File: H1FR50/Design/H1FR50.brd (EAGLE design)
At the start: 34.6 x 60 mm, 49 parts, among them J1 MOLEX_INC_0732511150MOLEX_INC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, P1 HEXABIT_17.32_X2_NO_P5, U1 STM32F091RBT6STMICROELECTRONI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, U2 TPS22943DCKR, U3 BGA824N6, U4 TESEO-LIV3F, U5 B39162B4327P810, X1 XTALL_CSTCE8M00G52

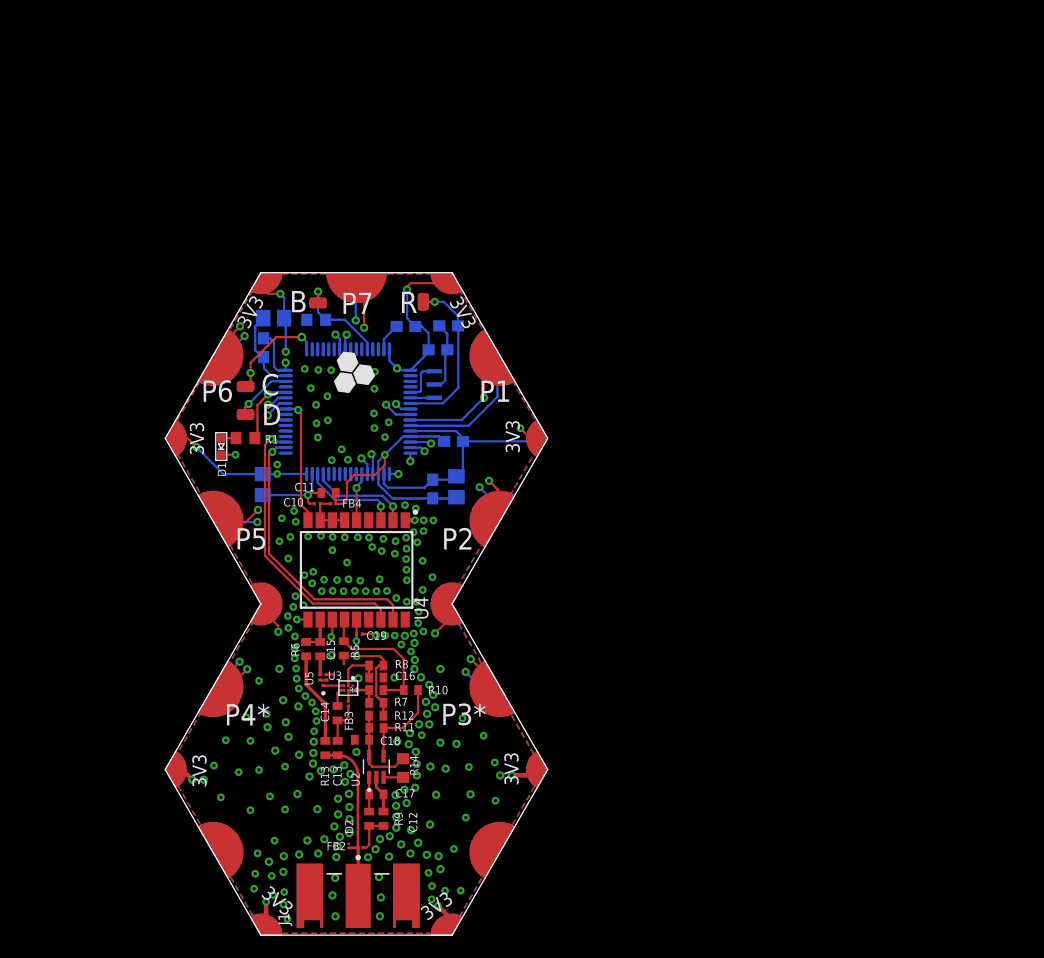
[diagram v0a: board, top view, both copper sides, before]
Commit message: -Changing the MC to STM32G0B1CEU6N -Changing the GPS Module to SAM-M8Q-0-10 u-blox
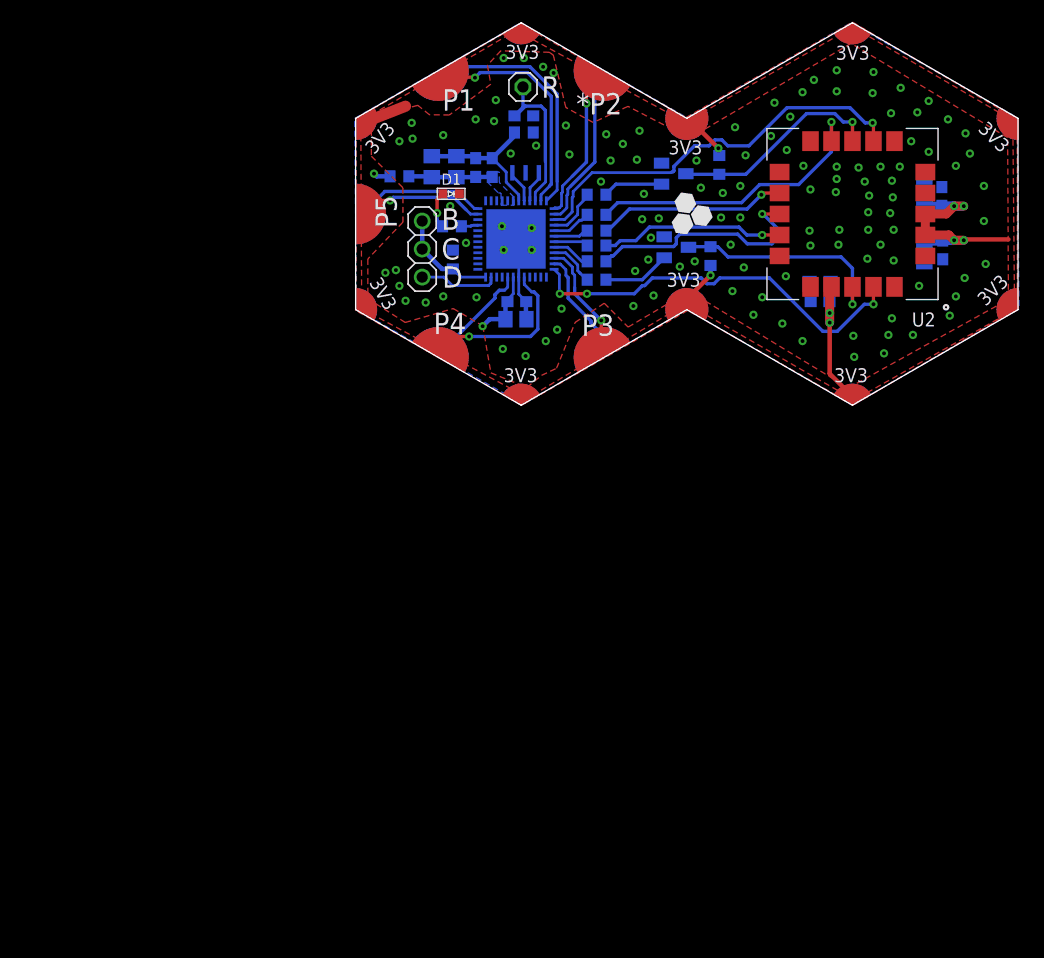
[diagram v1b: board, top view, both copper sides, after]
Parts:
- removed B, C, D, R: PAD1, Hexabitz:PAD1
- removed C14: 3.9pF, HEXABITZ_RCLS:C-0402
- removed C15: 120pF, HEXABITZ_RCLS:C-0402
- removed C16: 1nF, HEXABITZ_RCLS:C-0402
- removed C17: 1.00uF, HEXABITZ_RCLS:C-0402
- removed C18: 2.2uF, HEXABITZ_RCLS:C-0402
- removed C19: 56pF, HEXABITZ_RCLS:C-0201
- removed D2: ESDARF02-1BU2CK, HEXABITZ_RCLS:CAPC0201X13N
- removed FB4: 27nH, HEXABITZ_RCLS:FB-0402
- removed J1: MOLEX_INC_0732511150MOLEX_INC_0732511150_0_0, HEXABITZ_CONNECTION_PARTS:MOLEX_INC_0732511150_0
- removed P1: HEXABIT_17.32_X2_NO_P5, hexabitz_connectors:HEXABIT_17.32_X2_NO_P5
- removed R10, R12: 0.0R, HEXABITZ_RCLS:R-0402
- removed R11, R13: DNP, HEXABITZ_RCLS:R-0402
- removed R14: 100k, HEXABITZ_RCLS:R-0603
- removed U3: BGA824N6, HEXABITZ_ICs:BGA824N6
- removed U4: TESEO-LIV3F, HEXABITZ_ICs:SON110P970X1010X230-18N
- removed U5: B39162B4327P810, HEXABITZ_ICs:FIL_B39162B4327P810
- added FB1: (no value), HEXABITZ_RCLS:FB-0603
- added JP1: R, HEXABITZ_USER_INTERFACE_PARTS:1X01
- added JP2: (no value), pinhead:1X03
- added P2: HEXABIT_X2_P1_P5, hexabitz_connectors:HEXABIT_17.32_X2_P1_P5
- added Q1, Q2: MMBT3904LT1, HEXABITZ_RCLS:MMBT3904LT1
- added R3: 270R, HEXABITZ_RCLS:R-0603
- C1: value 10nF -> 100nF; device Hexabitz:C-0603 -> HEXABITZ_RCLS:C-0603
- C10: value 56pF -> 100nF; device HEXABITZ_RCLS:C-0201 -> HEXABITZ_RCLS:C-0603
- C11: value 10nF -> 4.7uF; device HEXABITZ_RCLS:C-0402 -> HEXABITZ_RCLS:C-0805-POL
- C12: value 56pF -> 100nF; device HEXABITZ_RCLS:C-0402 -> HEXABITZ_RCLS:C-0603
- C13: value 120pF -> 4.7uF; device HEXABITZ_RCLS:C-0402 -> HEXABITZ_RCLS:C-0805-POL
- C2: value 1.00uF -> 4.7uF; device Hexabitz:C-0805-POL -> HEXABITZ_RCLS:C-0805-POL
- C3, C5, C6, C8: device Hexabitz:C-0603 -> HEXABITZ_RCLS:C-0603
- C4: value 4.7uF -> 1uF; device Hexabitz:C-0805-POL -> HEXABITZ_RCLS:C-0805-POL
- C7: device Hexabitz:C-0805-POL -> HEXABITZ_RCLS:C-0805-POL
- C9: value 100nF -> 4.7uF; device Hexabitz:C-0603 -> HEXABITZ_RCLS:C-0805-POL
- FB2: value 56nH -> BLM18KG601SN1D; device HEXABITZ_RCLS:FB-0402 -> HEXABITZ_RCLS:FB-0603
- FB3: value 6.8nH -> BLM18KG601SN1D; device HEXABITZ_RCLS:FB-0402 -> HEXABITZ_RCLS:FB-0603
- R1: value 270.0R -> 10K; device Hexabitz:R-0603 -> HEXABITZ_RCLS:R-0603
- R2: value 10.0K -> 0.0R; device Hexabitz:R-0603 -> HEXABITZ_RCLS:R-0603
- R4: value 0.0R -> 10K; device HEXABITZ_RCLS:R-0402 -> HEXABITZ_RCLS:R-0603
- R5: value 10.0k -> 10K; device HEXABITZ_RCLS:R-0402 -> HEXABITZ_RCLS:R-0603
- R6, R7: value DNP -> 10K; device HEXABITZ_RCLS:R-0402 -> HEXABITZ_RCLS:R-0603
- R8: value 0.0R -> 150R; device HEXABITZ_RCLS:R-0402 -> HEXABITZ_RCLS:R-0603
- R9: value DNP -> 150R; device HEXABITZ_RCLS:R-0402 -> HEXABITZ_RCLS:R-0603
- U1: value STM32F091RBT6STMICROELECTRONICS_STM32F091RBT6_0_1 -> STM32G0B1CEU6NUFQFPN48_STM32_STM; device Hexabitz:STMICROELECTRONICS_STM32F091RBT6_1 -> HEXABITZ_ICs:UFQFPN48_STM32_STM
- U2: value TPS22943DCKR -> SAM-M8Q-0-10; device HEXABITZ_ICs:SOT65P210X110-5N -> SAM-M8Q-0-10:MODULE_SAM-M8Q-0-10
- moved U2 66.1 mm to (44.9, 20.3), turned to 180 degrees
- moved C10 63.0 mm to (53.0, 21.9), flipped to the bottom, turned to 90 degrees
- moved C12 61.3 mm to (42.0, 12.4), flipped to the bottom, turned to 0 degrees
- moved C13 60.6 mm to (42.0, 14.0), flipped to the bottom, turned to 0 degrees
- moved C11 60.3 mm to (51.4, 22.0), flipped to the bottom, turned to 90 degrees
- moved FB2 58.6 mm to (21.7, 17.5), flipped to the bottom, turned to 0 degrees
- moved R9 58.4 mm to (21.7, 20.2), flipped to the bottom, turned to 0 degrees
- moved R6 57.6 mm to (32.9, 24.8), flipped to the bottom
- moved R7 50.5 mm to (32.1, 16.5), flipped to the bottom, turned to 270 degrees
- moved R5 47.0 mm to (21.7, 22.1), flipped to the bottom, turned to 0 degrees
- moved FB3 45.9 mm to (21.7, 16.0), flipped to the bottom, turned to 0 degrees
- moved C8 45.3 mm to (53.1, 17.1), turned to 270 degrees
- moved C9 44.9 mm to (51.4, 16.9), turned to 270 degrees
- moved R8 44.2 mm to (21.7, 18.8), flipped to the bottom
- moved R4 42.2 mm to (21.7, 14.4), flipped to the bottom
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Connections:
- removed net ANTOFF: R10.2, R4.2, R5.1, U4.13
- removed net ANT_IN: R13.1, R6.1
- removed net B1: B.P$1, B.P$2, R2.2, U1.60
- removed net I2C_CLOCK: U1.34, U4.17
- removed net I2C_DATA: U1.35, U4.16
- removed net N$13: U3.3, U5.1
- removed net N$16: R4.1, R7.1, U3.6
- removed net N$17: C15.1, U5.4
- removed net N$19: C16.1, R8.1, U3.2
- removed net N$20: C17.1, R9.1, U2.1
- removed net N$22: R10.1, R11.2, U2.4
- removed net N$23: C18.1, R11.1, R12.2, R14.1, U2.5
- removed net R1: C8.1, R.P$1, R.P$2, U1.7
- removed net RF_IN: C15.2, R6.2, U4.11
- removed net SYS_RESET: U1.41, U4.9
- removed net SYS_WAKEUP: U1.22, U4.5
- removed net UART1_RX*: P1.PAD_PD7, U1.43
- removed net UART1_TX*: P1.PAD_PU7, U1.42
- removed net UART2_RX*: P1.PAD_PD3, U1.17
- removed net UART2_TX*: P1.PAD_PU3, U1.16
- removed net UART3_RX: U1.30, U4.3
- removed net UART3_TX: U1.29, U4.2
- removed net UART4_RX: P1.PAD_PD2, U1.15
- removed net UART4_TX: P1.PAD_PU2, U1.14
- removed net UART5_RX: P1.PAD_PD8, U1.56
- removed net UART5_TX: P1.PAD_PU8, U1.55
- removed net UART6_RX: P1.PAD_PD10, U1.21
- removed net UART6_TX: P1.PAD_PU10, U1.20
- removed net UART7_RX: P1.PAD_PD9, U1.9
- removed net UART7_TX: P1.PAD_PU9, U1.8
- removed net UART8_RX: P1.PAD_PD1, U1.11
- removed net UART8_TX: P1.PAD_PU1, U1.10
- removed net VCC_RF: C19.2, R12.1, R7.2, R8.2, U4.14
- removed net VCC_RF1: C10.2, FB4.1, U4.6, U4.7, U4.8
- new net C: JP2.1, JP2.2, R1.2, U1.36
- new net D: JP2.3, U1.35
- new net GPS_INT: U1.24, U2.19
- new net GPS_NRST: R4.2, U1.21
- new net GPS_SAFEBOOT: R5.2, U1.16
- new net GPS_SCL: R8.2, U1.18
- new net GPS_SDA: R9.2, U1.17
- new net GPS_TIMEPULSE: U1.15, U2.7
- new net GPS_UART_RX: FB2.2, U1.19
- new net GPS_UART_TX: FB3.2, U1.20
- new net N$14: R3.1, U1.45
- new net N$8: Q1.1, R5.1
- new net USART1_RX: P2.PAD_PD4, U1.32
- new net USART1_TX: P2.PAD_PU4, U1.29
- new net USART2_RX: P2.PAD_PD2, U1.14
- new net USART2_TX: P2.PAD_PU2, U1.13
- new net USART3_RX: P2.PAD_PD3, U1.23
- new net USART3_TX: P2.PAD_PU3, U1.22
- new net USART4_RX: P2.PAD_PD1, U1.12
- new net USART4_TX: P2.PAD_PU1, U1.11
- new net USART6_RX: P2.PAD_PD5, U1.48
- new net USART6_TX: P2.PAD_PU5, U1.47
- new net VDDA: C1.1, C2.1, C3.1, C4.1, FB1.1, U1.4, U1.5, U1.6
- new net VSSA: C1.2, C2.2, C3.2, C4.2, R2.1, U1.7
- net GND: now also C10.2, C11.2, C12.2, C13.2, P2.PAD_PD11, P2.PAD_PD12, P2.PAD_PD13, P2.PAD_PD14, P2.PAD_PD15, P2.PAD_PD16, P2.PAD_PD17, P2.PAD_PD18, P2.PAD_PD19, P2.PAD_PD20, Q1.2, Q2.2, R1.1, R2.2, U1.30, U1.49, U2.1, U2.10, U2.11, U2.15, U2.16, U2.20, U2.4, U2.5, U2.6; no longer C1.2, C10.1, C11.1, C12.1, C14.1, C16.2, C17.2, C18.2, C19.1, C2.2, C3.2, C4.2, D2.1, J1.2, J1.3, J1.4, J1.5, P1.PAD_PD11, P1.PAD_PD12, P1.PAD_PD13, P1.PAD_PD14, P1.PAD_PD15, P1.PAD_PD16, P1.PAD_PD17, P1.PAD_PD18, P1.PAD_PD19, P1.PAD_PD20, R2.1, R5.2, U1.12, U1.18, U1.31, U1.47, U1.63, U2.2, U3.1, U3.4, U4.1, U4.10, U4.12, U5.2, U5.3, U5.5
- net N$1: now also D1.A, R3.2; no longer C13.2, C14.2, FB3.1
- net N$10: now also FB3.1, U2.13; no longer R1.2, U1.44
- net N$11: now also R8.1, U2.12; no longer C12.2, FB2.1, R9.2
- net N$12: now also R9.1, U2.9; no longer FB3.2, U3.5
- net N$2: now also U1.8, X1.P$3; no longer R14.2, U2.3
- net N$3: now also U1.9, X1.P$1; no longer C13.1, D2.2, FB2.2, J1.1, R13.2
- net N$4: now also Q2.3, R7.1, U2.18; no longer D1.A, R1.1
- net N$5: now also C6.1, JP1.1, U1.10; no longer U1.5, X1.P$1
- net N$6: now also Q1.3, R6.1, U2.8; no longer U1.6, X1.P$3
- net N$7: now also Q2.1, R4.1; no longer D.P$1, D.P$2, U1.46
- net N$9: now also FB2.1, U2.14; no longer C.P$1, C.P$2, U1.49
- net VDD: now also C10.1, C11.1, C12.1, C13.1, C8.1, FB1.2, P2.PAD_PU11, P2.PAD_PU12, P2.PAD_PU13, P2.PAD_PU14, P2.PAD_PU15, P2.PAD_PU16, P2.PAD_PU17, P2.PAD_PU18, P2.PAD_PU19, P2.PAD_PU20, R6.2, R7.2, U1.31, U2.17, U2.2, U2.3; no longer C1.1, C11.2, C2.1, C3.1, C4.1, C6.1, FB4.2, P1.PAD_PU11, P1.PAD_PU12, P1.PAD_PU13, P1.PAD_PU14, P1.PAD_PU15, P1.PAD_PU16, P1.PAD_PU17, P1.PAD_PU18, P1.PAD_PU19, P1.PAD_PU20, U1.1, U1.13, U1.19, U1.32, U1.48, U1.64
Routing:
- net GND: track 63.2 -> 7.09 mm, vias 224 -> 121
- net VDD: track 92.9 -> 55.3 mm, vias 20 -> 10
- net GPS_TIMEPULSE: track 0.00 -> 37.0 mm, vias 0 -> 1
- net GPS_INT: track 0.00 -> 36.5 mm, vias 0 -> 3
- net UART1_RX*: track 31.0 -> 0.00 mm, vias 2 -> 0
- net UART1_TX*: track 30.7 -> 0.00 mm, vias 2 -> 0
- net UART7_TX: track 26.7 -> 0.00 mm, vias 2 -> 0
- net UART7_RX: track 26.3 -> 0.00 mm, vias 2 -> 0
- net N$12: track 0.99 -> 27.3 mm, vias 0 -> 1
- net I2C_DATA: track 25.7 -> 0.00 mm, vias 1 -> 0
- net UART5_RX: track 25.5 -> 0.00 mm, vias 2 -> 0
- net I2C_CLOCK: track 25.2 -> 0.00 mm, vias 1 -> 0
- net UART2_TX*: track 24.7 -> 0.00 mm, vias 2 -> 0
- net UART5_TX: track 24.6 -> 0.00 mm, vias 2 -> 0
- net UART2_RX*: track 24.5 -> 0.00 mm, vias 2 -> 0
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- added copper zone on layer 1, net VDD
- added copper zone on layer 16, net VDDA
- removed copper zone on layer 2, net GND
- removed copper zone on layer 15, net VDD
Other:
- board size 34.6 x 60 mm -> 60 x 34.6 mm
- board text added: "*P2"
- board text added: "P3"
- board text added: "P4"
- board text removed: "P2"
- board text removed: "P3*"
- board text removed: "P4*"
- board text removed: "P6"
- board text removed: "P7"
- board text removed: "Total Thickness 1.6 mm --------------------------------------------------------- copper_top_l1.gbr : Top Conductor - Copper: Thickness 0.035 mm Dielectric - FR-4: Thickness 0.175 mm copper_inner_l2.gbr : GND Plane - Copper: Thickness 0.035 mm Dielectric - FR-4: Thickness 1.11 mm copper_inner_l3.gbr : VDD Plane - Copper: Thickness 0.035 mm Dielectric - FR-4: Thickness 0.175 mm copper_bottom_l4.gbr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"

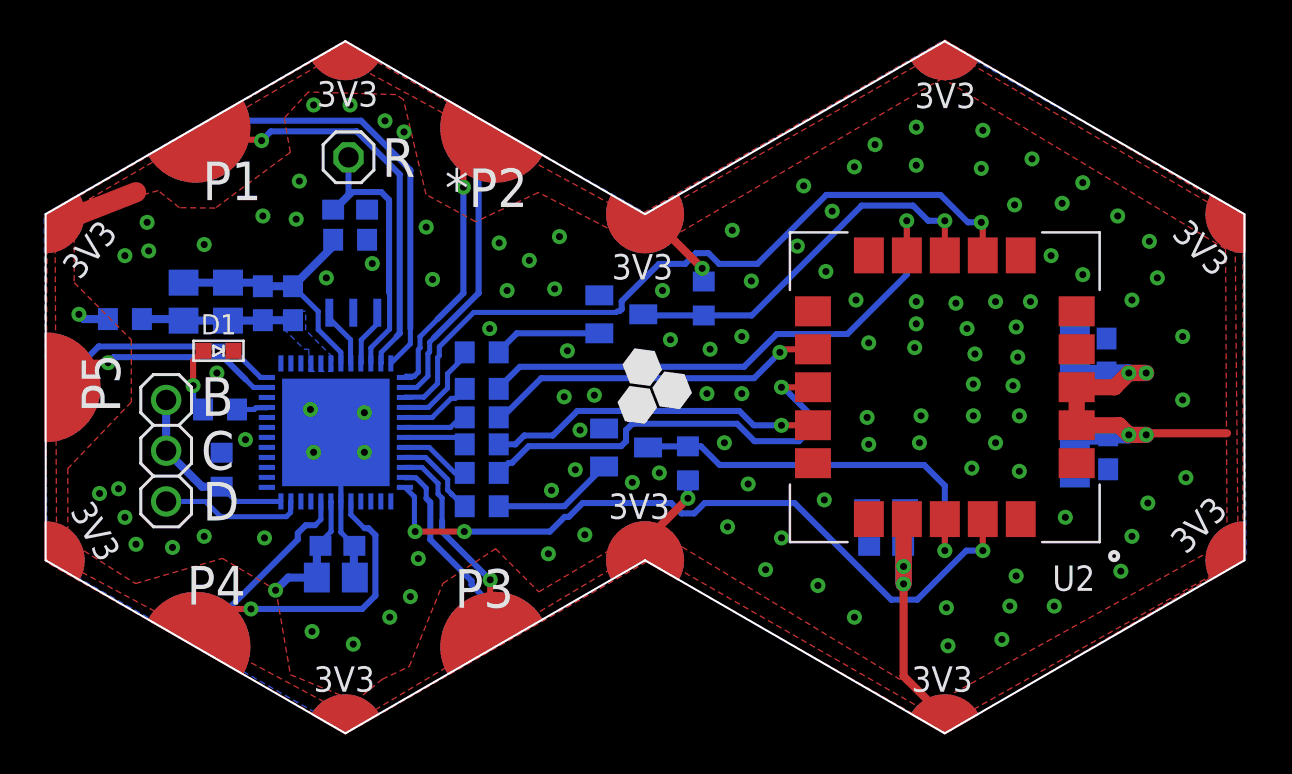
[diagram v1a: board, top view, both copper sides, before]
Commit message: -Changing the layout design to improve the performance
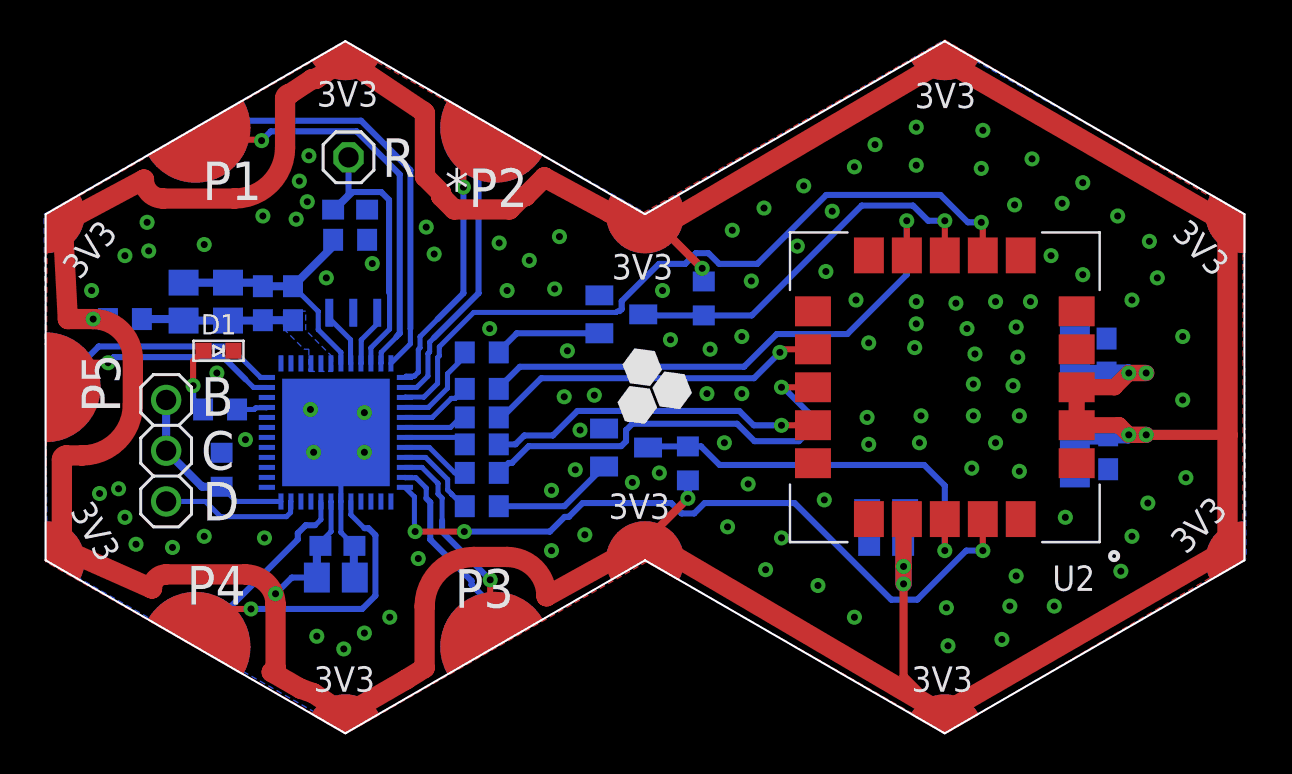
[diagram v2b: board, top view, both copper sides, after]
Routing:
- net VDD: track 55.3 -> 239.2 mm
- removed copper zone on layer 1, net VDD

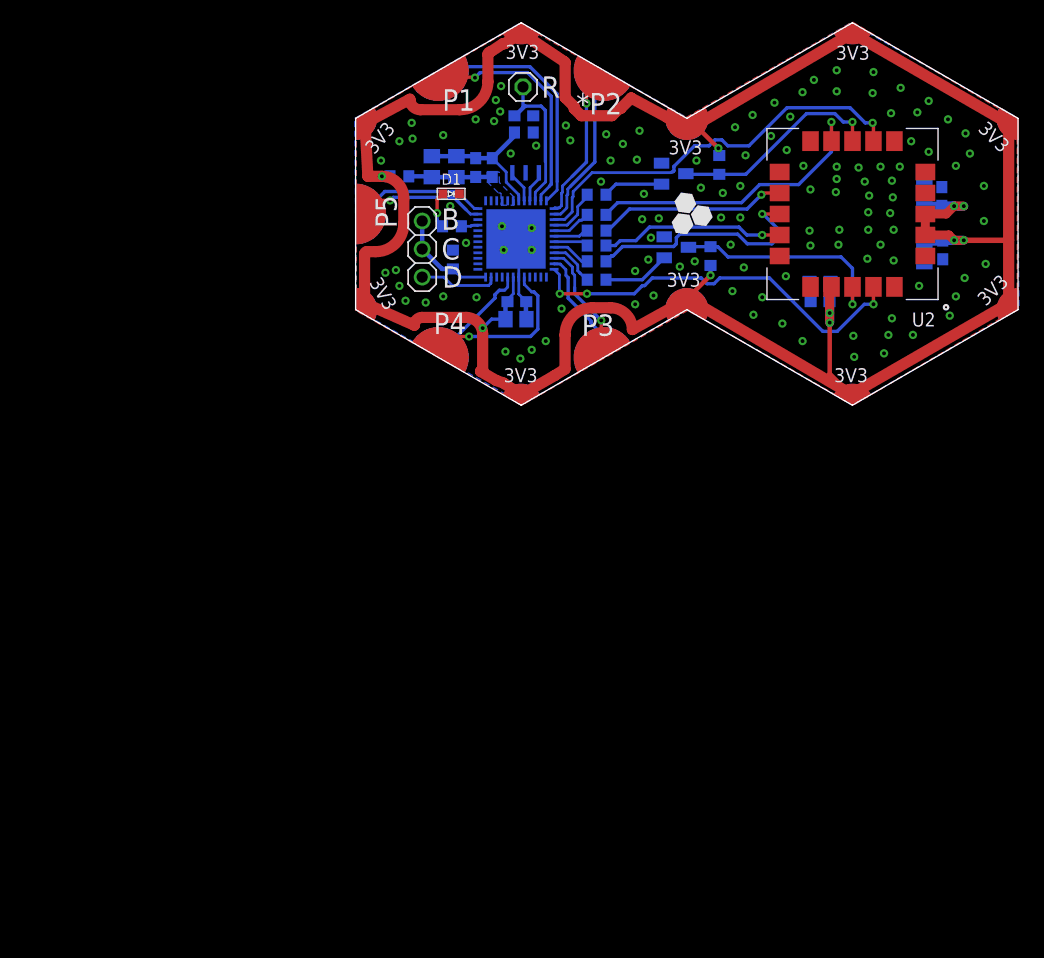
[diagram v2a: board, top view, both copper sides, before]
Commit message: -Correcting some documentaion issues
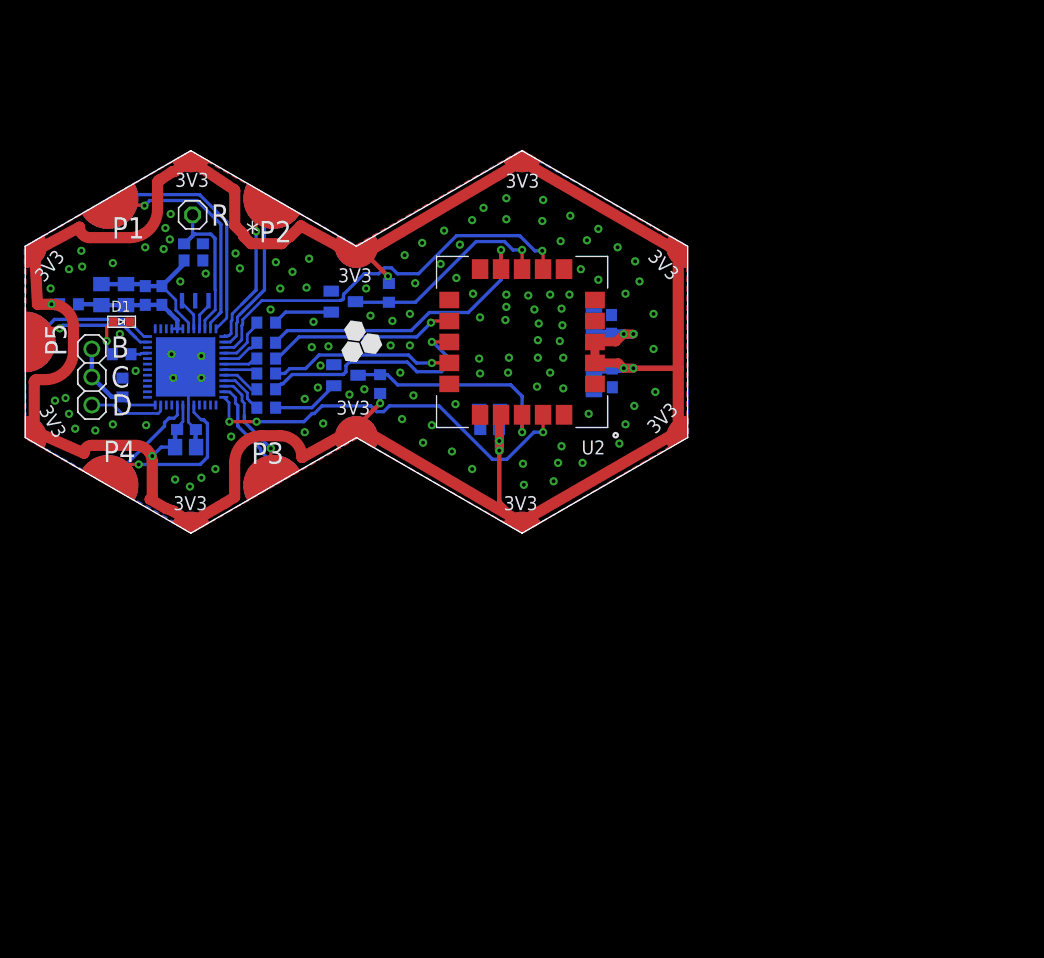
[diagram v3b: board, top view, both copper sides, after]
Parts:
- D1: value VLMS1300-GS08 -> RED; device Hexabitz:VLMS1300-GS08 -> HEXABITZ_USER_INTERFACE_PARTS:VLMS1300-GS08
- X1: value XTALL_CSTCE8M00G52 -> (none); device Hexabitz:XTALL_CSTCE8M00G52 -> HEXABITZ_RCLS:XTALL_CSTCE8M00G52
- moved C12 32.1 mm to (12.1, 0.79)
- moved C13 32.1 mm to (12.1, 2.38)
- moved U2 32.1 mm to (15.0, 8.73)
- moved C1 32.1 mm to (-19.1, 12.9)
- moved C10 32.1 mm to (23.1, 10.3)
- moved C11 32.1 mm to (21.5, 10.4)
- moved C2 32.1 mm to (-23.1, 13.0)
- moved C3 32.1 mm to (-17.6, 12.9)
- moved C4 32.1 mm to (-20.9, 13.0)
- moved C5 32.1 mm to (-15.4, 0.79)
- moved C6 32.1 mm to (-14.8, 17.6)
- moved C7 32.1 mm to (-15.5, -0.79)
- moved C8 32.1 mm to (23.2, 5.48)
- moved C9 32.1 mm to (21.5, 5.32)
- moved FB1 32.1 mm to (-26.0, 12.1)
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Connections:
- net N$2: now also X1.P$1; no longer X1.P$3
- net N$3: now also X1.P$3; no longer X1.P$1
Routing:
- net VDDA: track 7.60 -> 11.3 mm
- removed copper zone on layer 16, net VDDA
